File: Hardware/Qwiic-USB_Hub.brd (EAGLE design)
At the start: 43.2 x 81.3 mm, 98 parts, among them J1 USB_A_FEMALE, J2 Qwiic Right Angle, J3 PTH, J4 Qwiic Right Angle, J6 USB_A_FEMALE, J8 USB_A_FEMALE, J9 USB_A_FEMALE, Q1 4.3A/20V/54mΩ, Q2 4.3A/20V/54mΩ, Q3 4.3A/20V/54mΩ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

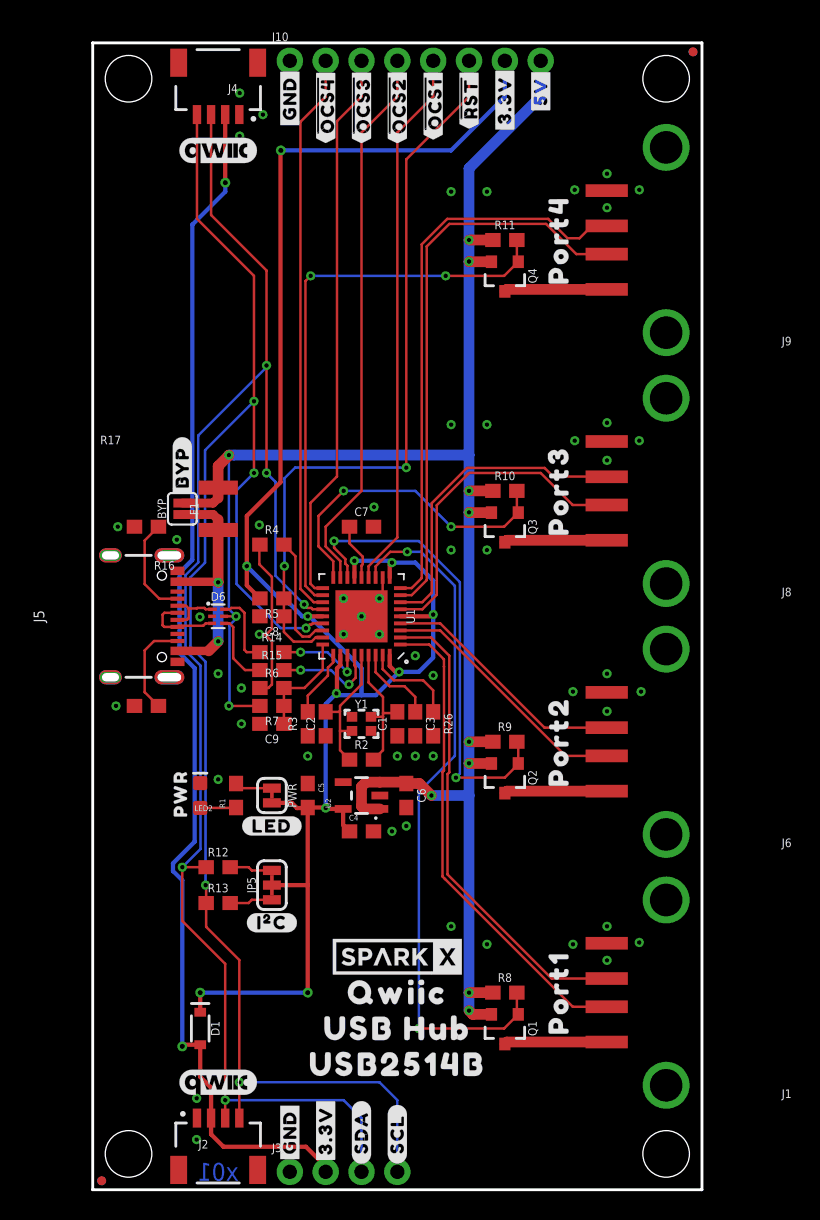
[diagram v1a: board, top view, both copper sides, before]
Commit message: Add connections to config pins.
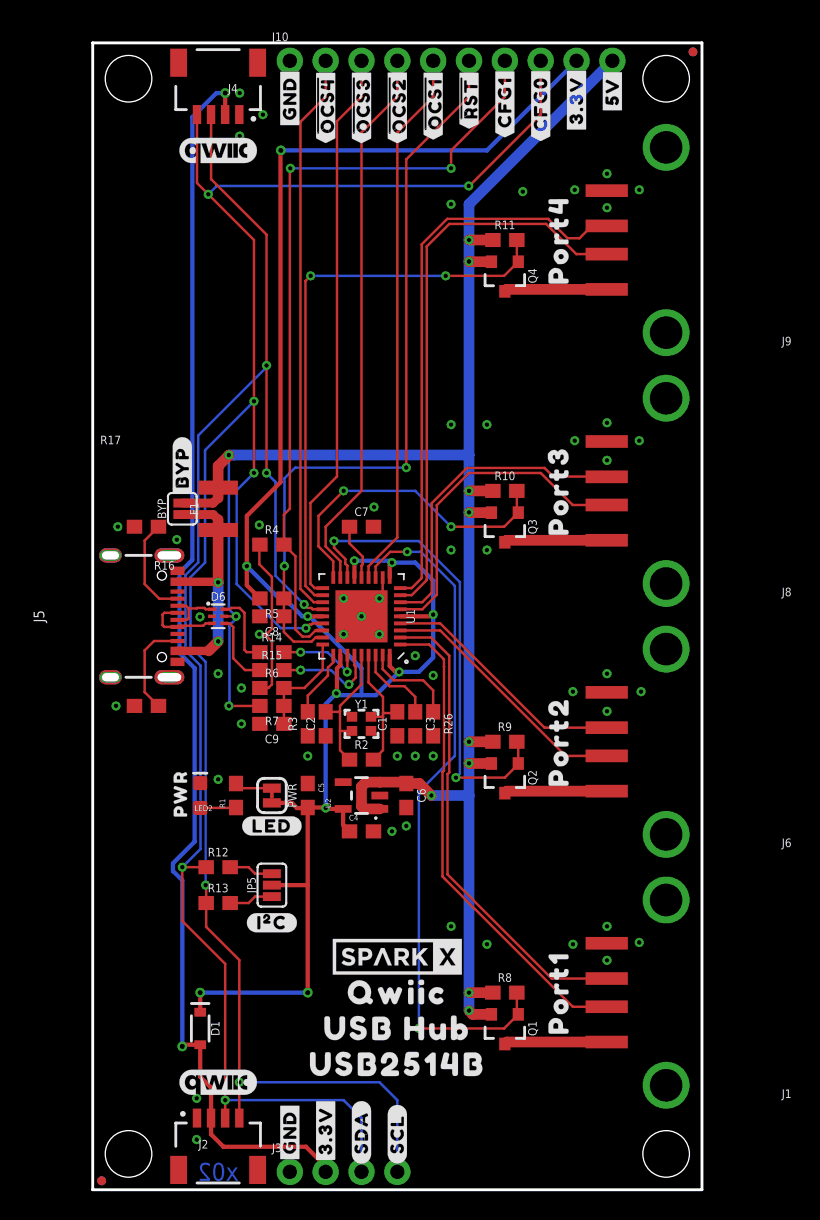
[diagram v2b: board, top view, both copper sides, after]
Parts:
- added U$24, U$29: (no value), output:#CFG0#1
- added U$25, U$28: (no value), output:#CFG1#0
- added U$30: (no value), output:##OCS1##3
- added U$43: (no value), output:##OCS2##2
- added U$44: (no value), output:##OCS3##1
- added U$45: (no value), output:##OCS4##0
- J10: device SparkFun-Connectors:1X08_NO_SILK -> SparkFun-Connectors:1X10_NO_SILK
- JP5: device SparkFun-Jumpers:SMT-JUMPER_3_2-NC_TRACE_SILK -> SparkFun-Jumpers:SMT-JUMPER_3_NO_SILK
- moved U$14 5.08 mm to (34.3, 77.2)
- moved U$15 5.08 mm to (36.8, 77.9)
- moved U$32 5.08 mm to (34.3, 77.2)
- moved U$37 5.08 mm to (36.8, 77.9)
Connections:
- removed net N$12: R4.2, U1.25
- removed net SCL: J2.4, J3.4, J4.4, R13.1, U1.24
- new net CFG1: J10.7, R4.2, U1.25
- new net SCL/CFG0: J10.8, J2.4, J3.4, J4.4, R13.1, U1.24
- net 3.3V: now also J10.9; no longer J10.7
- net 5V: now also J10.10; no longer J10.8
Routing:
- net SCL/CFG0: track 0.00 -> 143.6 mm, vias 0 -> 7
- net SCL: track 113.9 -> 0.00 mm, vias 5 -> 0
- net CFG1: track 0.00 -> 56.1 mm, vias 0 -> 2
- net N$12: track 8.67 -> 0.00 mm
- net 3.3V: track 136.2 -> 139.8 mm
- net N$21: track 86.2 -> 89.6 mm
- net 5V: track 138.1 -> 140.2 mm
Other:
- board text added: "x02"
- board text removed: "x01"
